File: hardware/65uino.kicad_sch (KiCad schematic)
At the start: 78 parts, among them J1 Barrel, J2 GPCO, J3 OLED, J4 USB2.0_16P, J5 Databus, J6 Chip select, J7 Addressbus, J8 Signals, SW1 RST, SW2 BTN, U1 R6507, U2 74HC161, U3 6532, U4 w27C512, U5 MIC5504-3.3YM5, U6 AMS1117-5.0, U7 SN74LVC1G14DBVR, U8 CH340G, U9 74HC138, X1 8MHz, Y2 12MHz

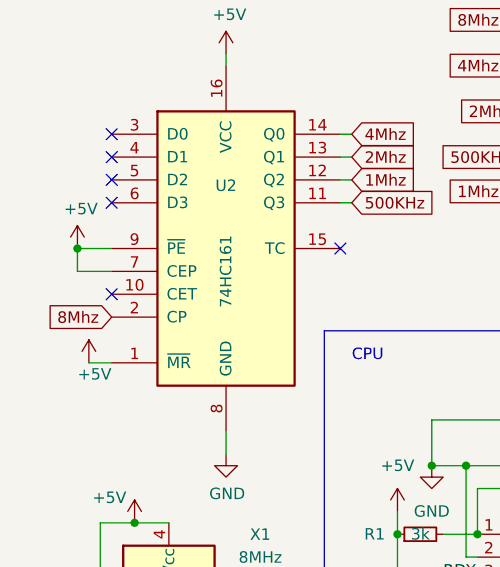
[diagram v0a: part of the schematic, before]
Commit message: Rev1 Gerber Fix
Connect U2 pin 9 and 10 for stable oscillator performance without solder blob
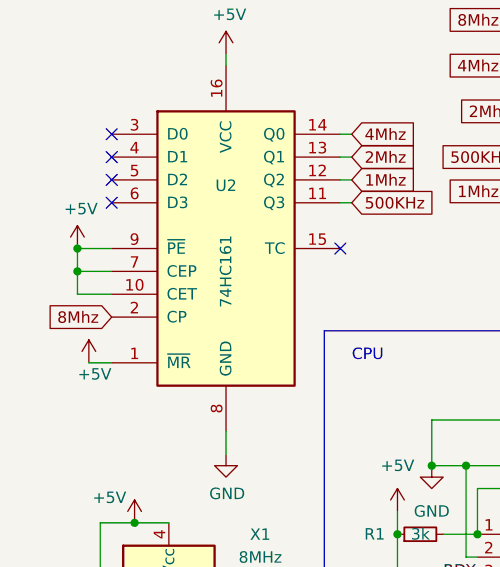
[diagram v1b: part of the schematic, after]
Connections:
- net +5V: now also U2.10 (CET)
- no-connect marks 18 -> 17
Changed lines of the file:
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@@
 	)
 	(junction
+		(at 17.78 114.3)
+		(diameter 0)
+		(color 0 0 0 0)
+	)
+	(junction
 		(at 62.23 143.51)
 		(diameter 0)
@@
 		(at 21.59 99.06)
 	)
-	(no_connect
-		(at 21.59 116.84)
-	)
 	(bus_entry
 		(at 92.71 158.75)
@@
 	(wire
 		(pts
+			(xy 17.78 116.84) (xy 21.59 116.84)
+		)
+		(stroke
+			(width 0)
+			(type default)
+		)
+	)
+	(wire
+		(pts
 			(xy 96.52 44.45) (xy 93.98 44.45)
 		)
@@
 		)
 		(stroke
+			(width 0)
+			(type default)
+		)
+	)
+	(wire
+		(pts
+			(xy 17.78 114.3) (xy 17.78 116.84)
+		)
+		(stroke
